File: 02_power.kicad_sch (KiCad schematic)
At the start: 0 parts

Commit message: Added USB-C, Battery Charging andOn/Off
Signed-off-by: Anna-Lena Marx <anna-lena.marx@web.de>
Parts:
- added C12, C13: 10uF, Capacitor_SMD:C_1206_3216Metric_Pad1.33x1.80mm_HandSolder, symbol Device:C
- added D4, D5: LED, LED_SMD:LED_1206_3216Metric_Pad1.42x1.75mm_HandSolder, symbol Device:LED
- added D6: MBR0530, Diode_SMD:D_SOD-123, symbol Diode:MBR0530
- added J5: UJ20-C-H-G-SMT-TR, UJ20:CUI_UJ20-C-H-G-SMT-TR, symbol UJ20-C-H-G-SMT-TR:UJ20-C-H-G-SMT-TR
- added J6: Conn_01x02_Socket, Connector_JST:JST_EH_S2B-EH_1x02_P2.50mm_Horizontal, symbol Connector:Conn_01x02_Socket
- added Q2: DMG2305UX-7, Package_TO_SOT_SMD:SOT91P240X110-3N_DMG2305UX-7, symbol Transistor_FET:DMG2305UX-7
- added R11: 2.7k, Resistor_SMD:R_1206_3216Metric_Pad1.30x1.75mm_HandSolder, symbol Device:R
- added R12: 2k, Resistor_SMD:R_1206_3216Metric_Pad1.30x1.75mm_HandSolder, symbol Device:R
- added R13, R14: 1.5k, Resistor_SMD:R_1206_3216Metric_Pad1.30x1.75mm_HandSolder, symbol Device:R
- added S2: 450404015514, 4504040015514:450404015514, symbol 450404015514:450404015514
- added TH1: Thermistor_NTC 10k, Resistor_SMD:R_1206_3216Metric_Pad1.30x1.75mm_HandSolder, symbol Device:Thermistor_NTC
- added U2: BQ24090DGQ, Package_SO:HVSSOP-10-1EP_3x3mm_P0.5mm_EP1.57x1.88mm_ThermalVias, symbol Battery_Management:BQ24090DGQ
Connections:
- new net: D4.1 (K), U2.5 (~{PG})
- new net: D4.2 (A), R13.2
- new net: R11.1, U2.2 (ISET)
- new net: R12.1, U2.4 (PRETERM)
- new net: D5.1 (K), U2.8 (~{CHG})
- new net: TH1.1, U2.9 (TS)
- new net: D5.2 (A), R14.2
- new net GND: C12.2, C13.2, J5.A1 (GND), J5.A12 (GND), J5.B1 (GND), J5.B12 (GND), J5.SH1 (SHIELD), J5.SH2 (SHIELD), J5.SH3 (SHIELD), J5.SH4 (SHIELD), J6.2 (Pin_2), R11.2, R12.2, S2.1, TH1.2, U2.11 (VSS), U2.3 (VSS), U2.7 (ISET2)
- new net USB_VBUS: C12.1, J5.A4 (VBUS), J5.A9 (VBUS), J5.B4 (VBUS), J5.B9 (VBUS), U2.1 (IN)
- new net VBUS: Q2.1
- new net VSYS: S2.2
- new net V_USB_LIPO: C13.1, D6.1 (K), D6.2 (A), J6.1 (Pin_1), Q2.2, Q2.3, R13.1, R14.1, S2.3, U2.10 (OUT)
- no-connect marks 0 -> 8
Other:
- note added: "Charger connected (Power Good)"
- note added: "Charging Off for refresh charging"
- note added: "LiPo"
- note added: "Programs the fast charge current 2.7k -> 200mA"
- note added: "Programs the termination current threshold"

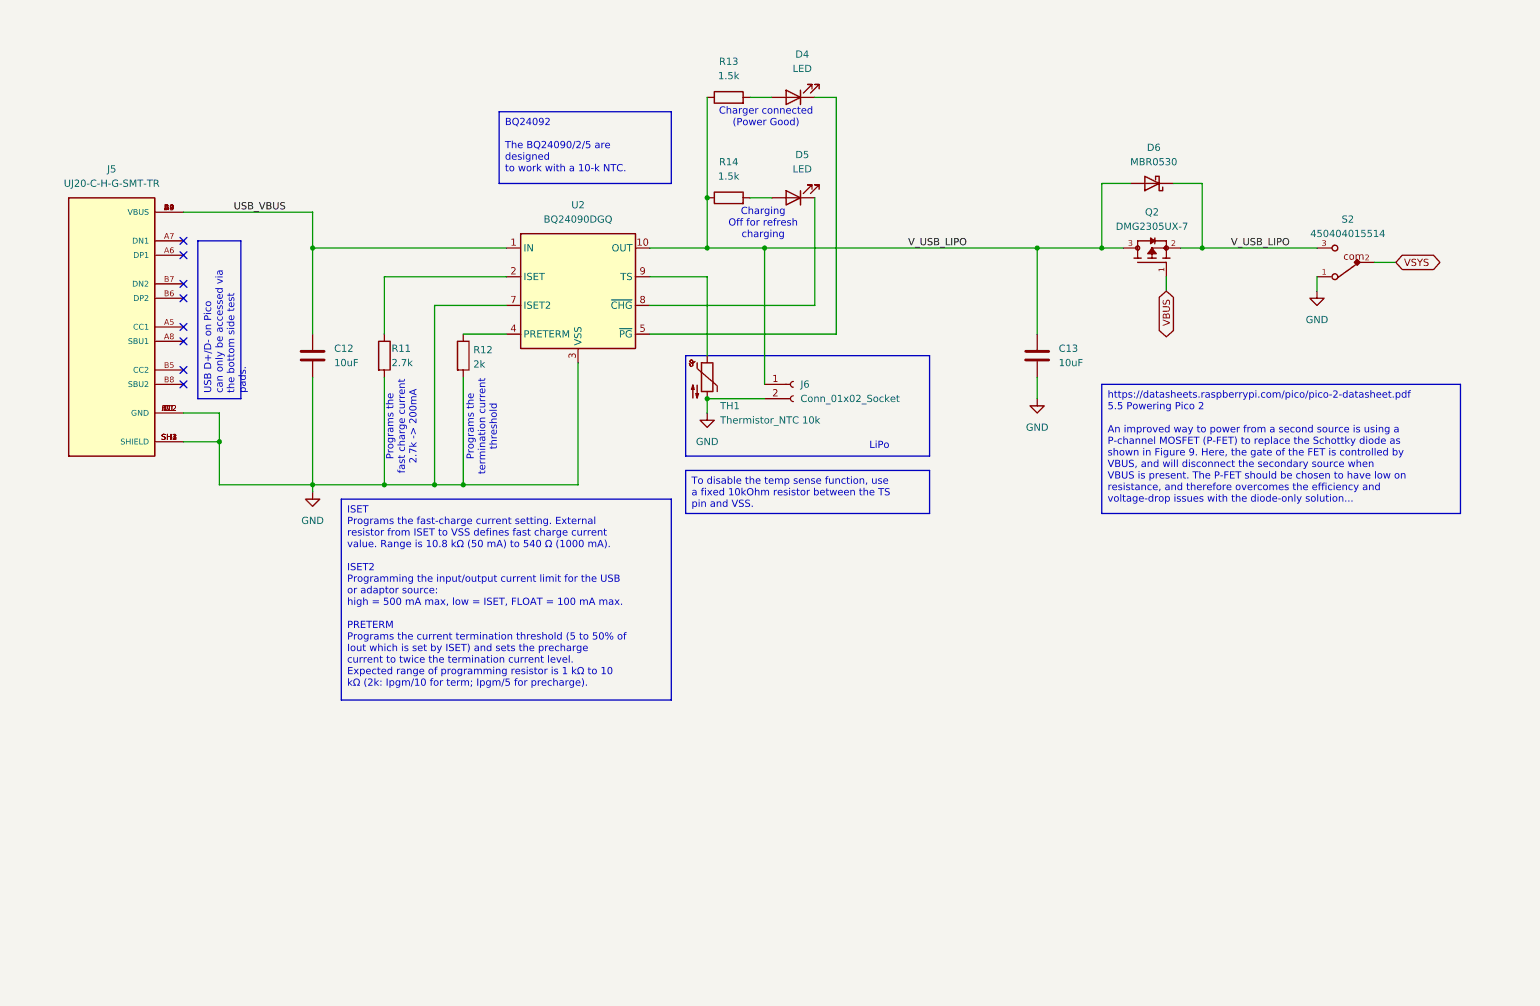
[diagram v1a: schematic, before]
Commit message: Added some more notes, testpoints and rechecked footprints and parts
Signed-off-by: Anna-Lena Marx <anna-lena.marx@web.de>
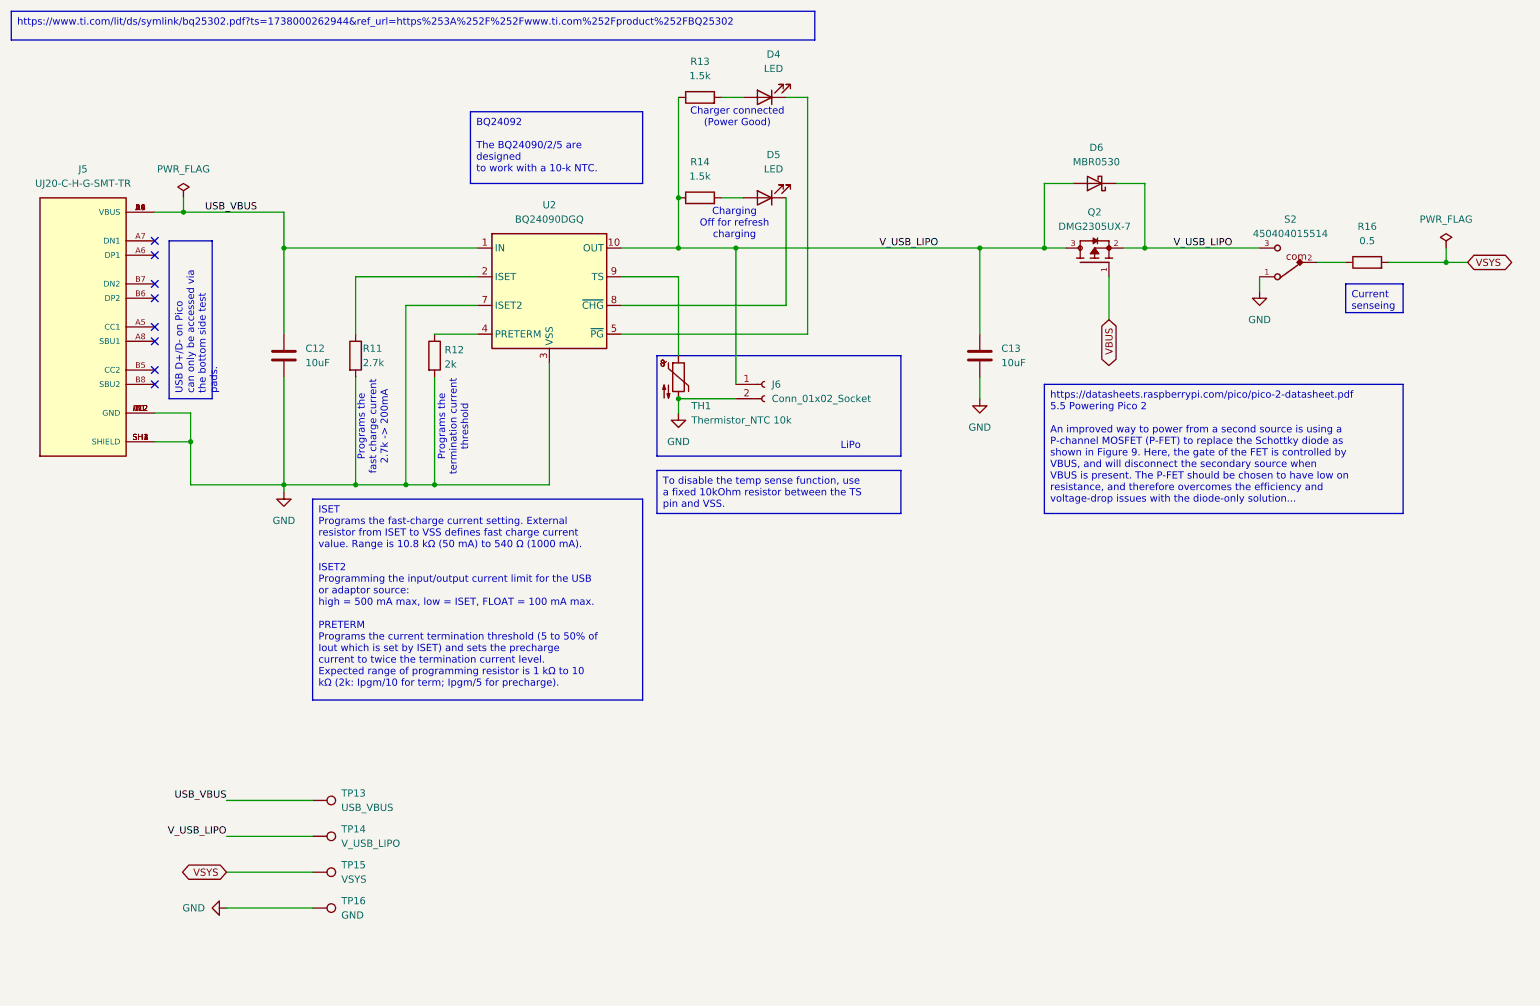
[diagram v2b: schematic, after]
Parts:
- added R16: 0.5, Resistor_SMD:R_1206_3216Metric_Pad1.30x1.75mm_HandSolder, symbol Device:R
- added TP13: USB_VBUS, TestPoint:TestPoint_Pad_D2.5mm, symbol Connector:TestPoint
- added TP14: V_USB_LIPO, TestPoint:TestPoint_Pad_D2.5mm, symbol Connector:TestPoint
- added TP15: VSYS, TestPoint:TestPoint_Pad_D2.5mm, symbol Connector:TestPoint
- added TP16: GND, TestPoint:TestPoint_Pad_D2.5mm, symbol Connector:TestPoint
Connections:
- net GND: now also TP16.1
- net USB_VBUS: now also TP13.1
- net VSYS: now also R16.2, TP15.1; no longer S2.2
- net V_USB_LIPO: now also TP14.1
- new net: R16.1, S2.2
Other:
- moved on the sheet: C12, C13, D4, D5, D6, J5, J6, Q2, R11, R12, R13, R14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

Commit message: Changed buttons to smaller ones, updated some comments
Signed-off-by: Anna-Lena Marx <anna-lena.marx@web.de>
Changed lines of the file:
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@@
+		)
+	)
+	(text_box "The final design shall contain the RP2350 directly, without the Pico2 breakout.\nThis connector should then also handle D+/D-.\nFor now, this connector would not be needed, but integrating it now helps getting used to it."
+		(exclude_from_sim no)
+		(at 15.24 101.6 0)
+		(size 40.64 17.78)
+		(stroke
+			(width 0)
+			(type default)
+		)
+		(fill
+			(type none)
+		)
+		(effects
+			(font
+				(size 1.27 1.27)
+			)
+			(justify left top)
 		)
 	)

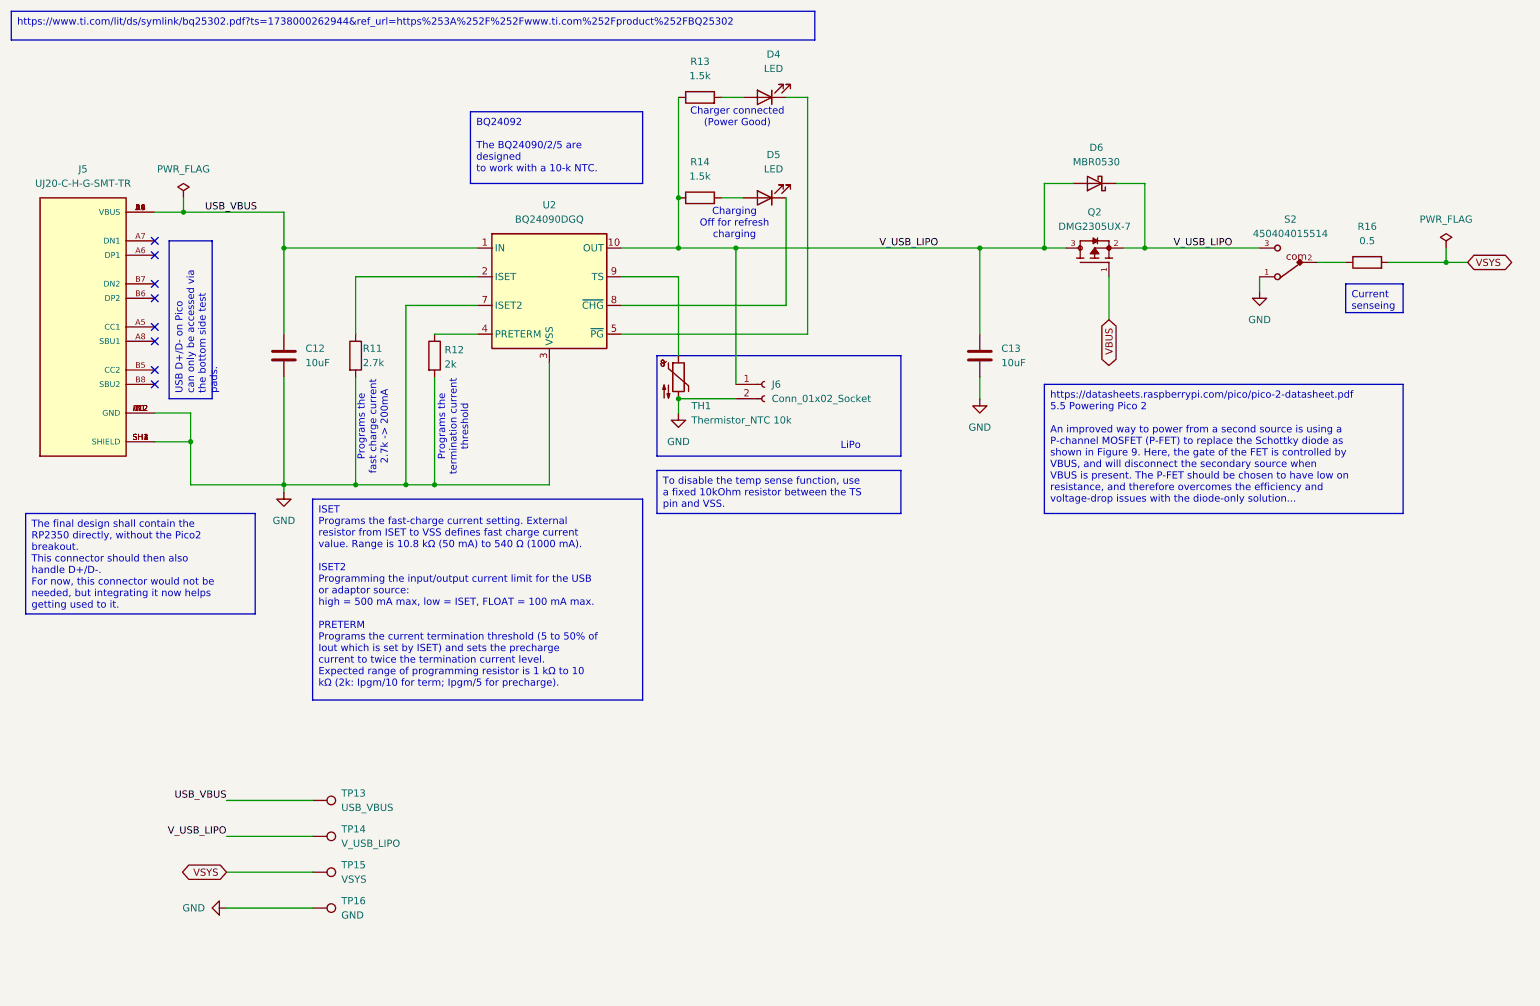
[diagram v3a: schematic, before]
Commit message: Added CC line pulldown resistors
Signed-off-by: Anna-Lena Marx <anna-lena.marx@web.de>
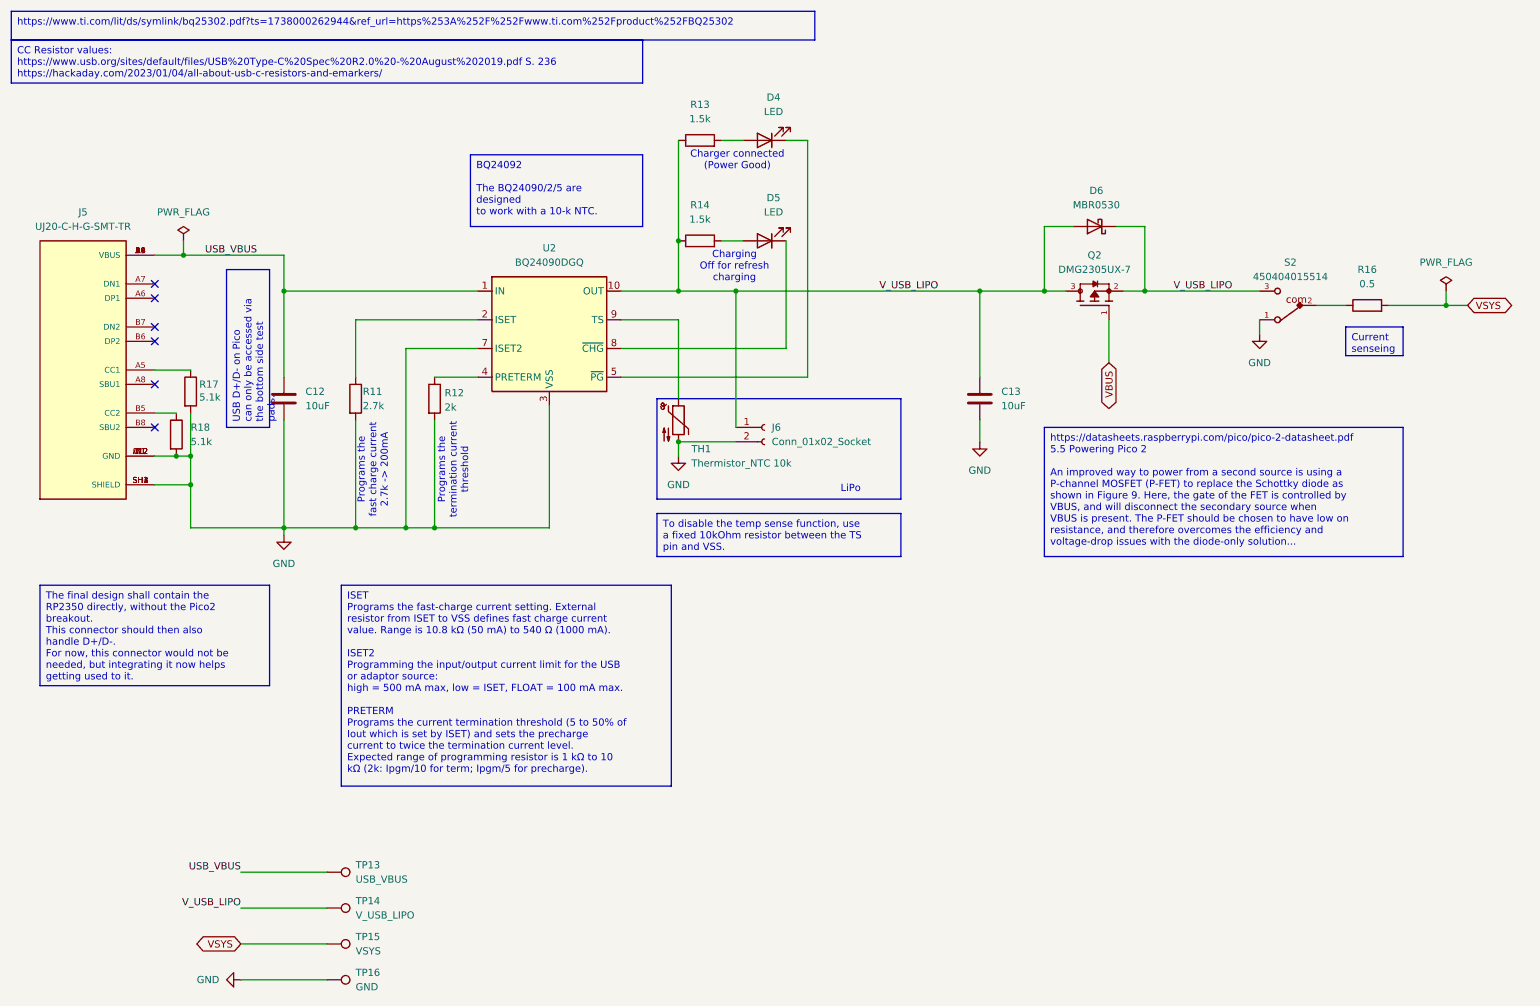
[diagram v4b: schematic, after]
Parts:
- added R17, R18: 5.1k, Resistor_SMD:R_1206_3216Metric_Pad1.30x1.75mm_HandSolder, symbol Device:R
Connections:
- net GND: now also R17.2, R18.2
- net at J5.A5 (CC1): now also R17.1
- net at J5.B5 (CC2): now also R18.1
- no-connect marks 8 -> 6
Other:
- moved on the sheet: C12, C13, D4, D5, D6, J5, J6, Q2, R11, R12, R13, R14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

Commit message: fix selfcontained and kibot output
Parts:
- J5: footprint UJ20:CUI_UJ20-C-H-G-SMT-TR -> prj-footprints:CUI_UJ20-C-H-C-3-SMT-TR
- Q2: footprint Package_TO_SOT_SMD:SOT91P240X110-3N_DMG2305UX-7 -> prj-footprints:SOT91P240X110-3N_DMG2305UX-7
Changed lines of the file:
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@@
 			)
 		)
-		(property "Footprint" "Package_TO_SOT_SMD:SOT91P240X110-3N_DMG2305UX-7"
+		(property "Footprint" "prj-footprints:SOT91P240X110-3N_DMG2305UX-7"
 			(at 204.47 64.77 0)
 			(effects
@@
 			)
 		)
-		(property "Footprint" "UJ20:CUI_UJ20-C-H-G-SMT-TR"
+		(property "Footprint" "prj-footprints:CUI_UJ20-C-H-C-3-SMT-TR"
 			(at 25.4 76.2 0)
 			(effects

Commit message: switched to self-contained symbols, update kibot conf
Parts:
- removed Q2: DMG2305UX-7, prj-footprints:SOT91P240X110-3N_DMG2305UX-7, symbol Transistor_FET:DMG2305UX-7
- added Q2: DMG2305UX-7, DMG2305UX-7:SOT91P240X110-3N_DMG2305UX-7, symbol DMG2305UX-7:DMG2305UX-7
- J5: footprint prj-footprints:CUI_UJ20-C-H-C-3-SMT-TR -> UJ20-C-H-G-SMT-TR:CUI_UJ20-C-H-G-SMT-TR
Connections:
- net VBUS: now also Q2.1
- net V_USB_LIPO: now also Q2.2, Q2.3

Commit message: fix selfcontainment issues, added 2D rendering
Signed-off-by: Anna-Lena Marx <anna-lena.marx@web.de>
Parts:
- J5: footprint UJ20-C-H-G-SMT-TR:CUI_UJ20-C-H-G-SMT-TR -> prj-footprints:CUI_UJ20-C-H-G-SMT-TR
- Q2: footprint DMG2305UX-7:SOT91P240X110-3N_DMG2305UX-7 -> prj-footprints:SOT91P240X110-3N_DMG2305UX-7
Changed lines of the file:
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@@
 			)
 		)
-		(property "Footprint" "DMG2305UX-7:SOT91P240X110-3N_DMG2305UX-7"
+		(property "Footprint" "prj-footprints:SOT91P240X110-3N_DMG2305UX-7"
 			(at 204.47 64.77 0)
 			(effects
@@
 			)
 		)
-		(property "Footprint" "UJ20-C-H-G-SMT-TR:CUI_UJ20-C-H-G-SMT-TR"
+		(property "Footprint" "prj-footprints:CUI_UJ20-C-H-G-SMT-TR"
 			(at 25.4 76.2 0)
 			(effects
